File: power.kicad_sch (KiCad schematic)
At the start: 160 parts, among them Q10 SI7613DN-T1-GE3, Q2 BC817-25W, Q3 DZDH0401DW, Q4 DZDH0401DW, Q5 SI7613DN-T1-GE3, Q6 SI7613DN-T1-GE3, Q8 BC817-25W, U1 LT8350RV#PBF, U11 AP22615A_TSOT26, U2 MP2386GG, U3 TPS65983BAZBHR, U9 LM1117MP-3.3_NOPB

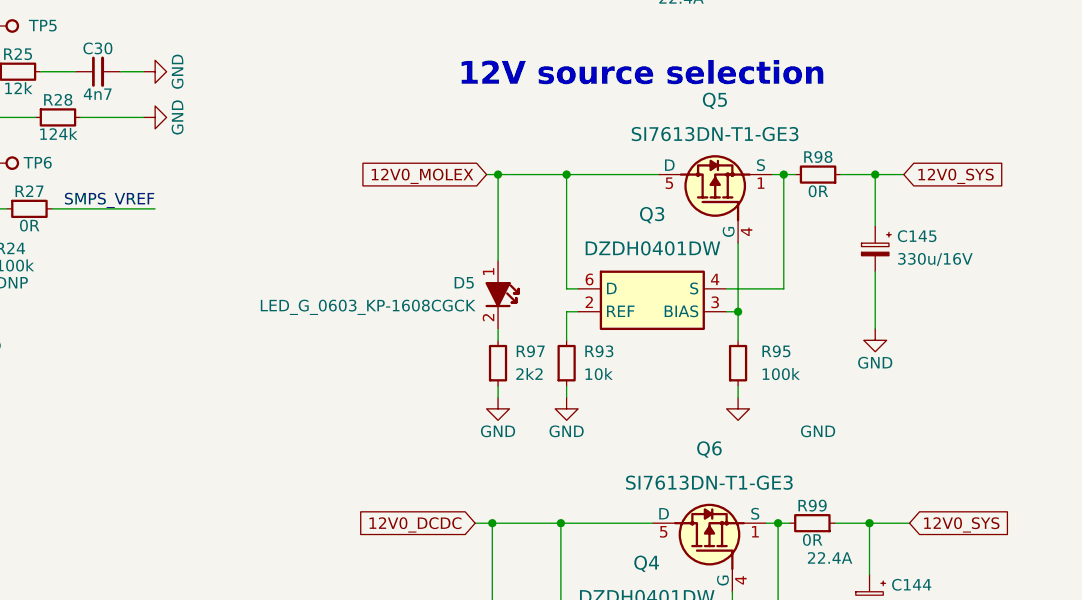
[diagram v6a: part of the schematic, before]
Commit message: Add filtration to 12V0_MOLEX
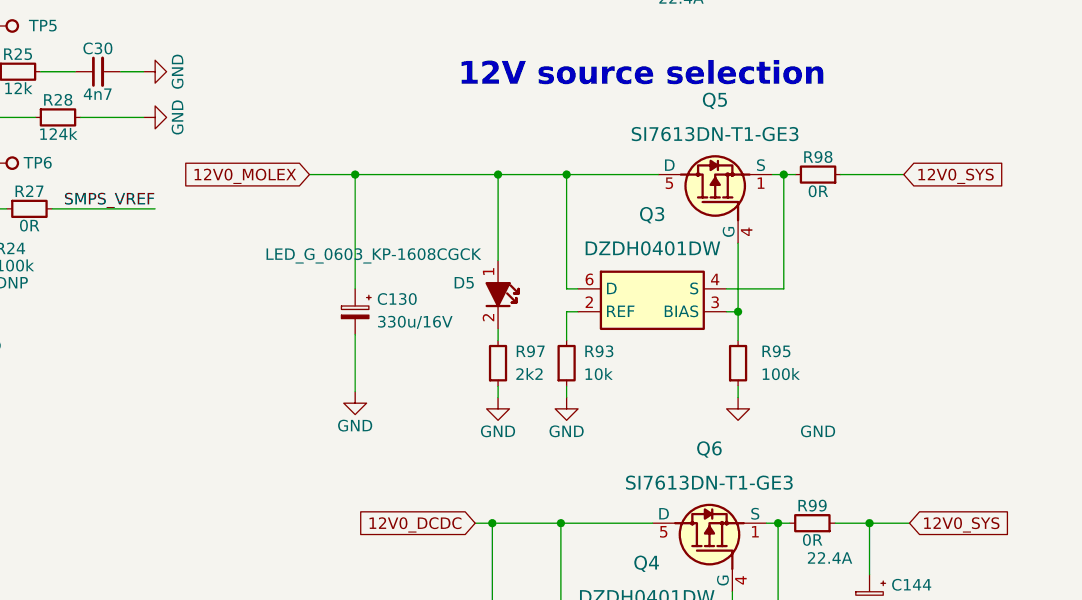
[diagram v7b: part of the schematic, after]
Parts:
- removed C145: C_Pol_330u_16V_KYOCERA-AVX-TCJ-E, antmicro-footprints:C_Pol_EIA-E, symbol antmicroCapacitorspol:C_Pol_330u_16V_KYOCERA-AVX-TCJ-E
- added C130: C_Pol_330u_16V_KYOCERA-AVX-TCJ-E, antmicro-footprints:C_Pol_EIA-E, symbol antmicroCapacitorspol:C_Pol_330u_16V_KYOCERA-AVX-TCJ-E
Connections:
- net 12V0_MOLEX: now also C130.1
- net GND: now also C130.2
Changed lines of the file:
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@@
   (junction (at 118.745 233.045) (diameter 0) (color 0 0 0 0)
   )
+  (junction (at 208.28 262.255) (diameter 0) (color 0 0 0 0)
+  )
   (junction (at 40.005 67.31) (diameter 0) (color 0 0 0 0)
   )
@@
   (junction (at 72.39 46.99) (diameter 0) (color 0 0 0 0)
   )
-  (junction (at 266.065 262.255) (diameter 0) (color 0 0 0 0)
-  )
   (junction (at 85.09 349.25) (diameter 0) (color 0 0 0 0)
   )
@@
   (no_connect (at 73.025 128.27))
   (no_connect (at 107.315 33.02))
+  (wire (pts (xy 208.28 262.255) (xy 224.155 262.255))
+    (stroke (width 0) (type default) (color 0 0 0 0))
+  )
   (wire (pts (xy 259.715 90.805) (xy 259.715 94.615))
     (stroke (width 0) (type default) (color 0 0 0 0))
@@
     (stroke (width 0) (type default) (color 0 0 0 0))
   )
+  (wire (pts (xy 208.28 280.035) (xy 208.28 286.385))
+    (stroke (width 0) (type default) (color 0 0 0 0))
+  )
   (wire (pts (xy 139.7 346.71) (xy 150.495 346.71))
     (stroke (width 0) (type default) (color 0 0 0 0))
@@
     (stroke (width 0) (type default) (color 0 0 0 0))
   )
-  (wire (pts (xy 222.885 262.255) (xy 224.155 262.255))
+  (wire (pts (xy 203.2 262.255) (xy 208.28 262.255))
     (stroke (width 0) (type default) (color 0 0 0 0))
   )
@@
     (stroke (width 0) (type default) (color 0 0 0 0))
   )
-  (wire (pts (xy 266.065 262.255) (xy 269.24 262.255))
-    (stroke (width 0) (type default) (color 0 0 0 0))
-  )
   (wire (pts (xy 220.98 33.02) (xy 232.41 33.02))
     (stroke (width 0) (type default) (color 0 0 0 0))
@@
     (stroke (width 0) (type default) (color 0 0 0 0))
   )
+  (wire (pts (xy 208.28 262.255) (xy 208.28 274.955))
+    (stroke (width 0) (type default) (color 0 0 0 0))
+  )
   (wire (pts (xy 61.595 209.55) (xy 61.595 211.455))
     (stroke (width 0) (type default) (color 0 0 0 0))
@@
     (stroke (width 0) (type default) (color 0 0 0 0))
   )
-  (wire (pts (xy 266.065 273.05) (xy 266.065 279.4))
-    (stroke (width 0) (type default) (color 0 0 0 0))
-  )
   (wire (pts (xy 99.06 253.365) (xy 100.965 253.365))
     (stroke (width 0) (type default) (color 0 0 0 0))
@@
     (stroke (width 0) (type default) (color 0 0 0 0))
   )
-  (wire (pts (xy 262.255 262.255) (xy 266.065 262.255))
+  (wire (pts (xy 262.255 262.255) (xy 269.24 262.255))
     (stroke (width 0) (type default) (color 0 0 0 0))
   )
@@
     (stroke (width 0) (type default) (color 0 0 0 0))
   )
-  (wire (pts (xy 266.065 262.255) (xy 266.065 267.97))
-    (stroke (width 0) (type default) (color 0 0 0 0))
-  )
   (wire (pts (xy 172.72 72.39) (xy 180.34 72.39))
     (stroke (width 0) (type default) (color 0 0 0 0))
@@
     (effects (font (size 1.27 1.27)) (justify left bottom))
   )
-  (global_label "12V0_MOLEX" (shape input) (at 222.885 262.255 180) (fields_autoplaced)
+  (global_label "12V0_MOLEX" (shape input) (at 203.2 262.255 180) (fields_autoplaced)
     (effects (font (size 1.27 1.27)) (justify right))
-    (property "Intersheet References" "${INTERSHEET_REFS}" (id 0) (at 208.6186 262.3344 0)
+    (property "Intersheet References" "${INTERSHEET_REFS}" (id 0) (at 188.9336 262.3344 0)
       (effects (font (size 1.27 1.27)) (justify right) hide)
     )
@@
   )
   (symbol (lib_name "LED_G_0603_KP-1608CGCK_2") (lib_id "thunderbolt-gpu-adapter:LED_G_0603_KP-1608CGCK") (at 224.155 271.78 270) (unit 1)
-    (in_bom yes) (on_board yes) (fields_autoplaced)
+    (in_bom yes) (on_board yes)
     (property "Reference" "D5" (id 0) (at 221.615 274.3199 90)
       (effects (font (size 1.27 1.27) (thickness 0.15)) (justify right))
     )
-    (property "Value" "LED_G_0603_KP-1608CGCK" (id 1) (at 221.615 276.8599 90)
+    (property "Value" "LED_G_0603_KP-1608CGCK" (id 1) (at 222.25 271.145 90)
       (effects (font (size 1.27 1.27) (thickness 0.15)) (justify right))
     )
@@
     (pin "2")
   )
+  (symbol (lib_id "antmicroCapacitorspol:C_Pol_330u_16V_KYOCERA-AVX-TCJ-E") (at 208.28 274.955 270) (unit 1)
+    (in_bom yes) (on_board yes) (fields_autoplaced)
+    (property "Reference" "C130" (id 0) (at 210.693 276.131 90)
+      (effects (font (size 1.27 1.27) (thickness 0.15)) (justify left))
+    )
+    (property "Value" "C_Pol_330u_16V_KYOCERA-AVX-TCJ-E" (id 1) (at 205.74 288.925 0)
+      (effects (font (size 1.27 1.27) (thickness 0.15)) (justify left bottom) hide)
+    )
+    (property "Footprint" "antmicro-footprints:C_Pol_EIA-E" (id 2) (at 200.66 288.925 0)
+      (effects (font (size 1.27 1.27) (thickness 0.15)) (justify left bottom) hide)
+    )
+    (property "Datasheet" "https://datasheets.kyocera-avx.com/TCJ.pdf" (id 3) (at 198.12 288.925 0)
+      (effects (font (size 1.27 1.27) (thickness 0.15)) (justify left bottom) hide)
+    )
+    (property "Val" "330u/16V" (id 4) (at 210.693 278.6547 90)
+      (effects (font (size 1.27 1.27) (thickness 0.15)) (justify left))
+    )
+    (property "MPN" "TCJE337M016R0070E" (id 5) (at 195.58 288.925 0)
+      (effects (font (size 1.27 1.27) (thickness 0.15)) (justify left bottom) hide)
+    )
+    (property "Manufacturer" "KYOCERA AVX" (id 6) (at 193.04 288.925 0)
+      (effects (font (size 1.27 1.27) (thickness 0.15)) (justify left bottom) hide)
+    )
+    (property "License" "Apache-2.0" (id 7) (at 190.5 288.925 0)
+      (effects (font (size 1.27 1.27) (thickness 0.15)) (justify left bottom) hide)
+    )
+    (property "Author" "Antmicro" (id 8) (at 187.96 288.925 0)
+      (effects (font (size 1.27 1.27) (thickness 0.15)) (justify left bottom) hide)
+    )
+    (property "Voltage" "16V" (id 9) (at 185.42 288.925 0)
+      (effects (font (size 1.27 1.27)) (justify left bottom) hide)
+    )
+    (property "Dielectric" "template_dielectric" (id 10) (at 182.88 288.925 0)
+      (effects (font (size 1.27 1.27)) (justify left bottom) hide)
+    )
+    (pin "1")
+    (pin "2")
+  )
   (symbol (lib_name "TP_1mm_SMD_6") (lib_id "thunderbolt-gpu-adapter:TP_1mm_SMD") (at 74.295 328.93 90) (unit 1)
     (in_bom yes) (on_board yes)
@@
     (pin "1")
   )
+  (symbol (lib_id "thunderbolt-gpu-adapter:GND") (at 208.28 286.385 0) (unit 1)
+    (in_bom yes) (on_board yes)
+    (property "Reference" "#PWR0197" (id 0) (at 208.28 292.735 0)
+      (effects (font (size 1.27 1.27)) hide)
+    )
+    (property "Value" "GND" (id 1) (at 208.28 290.195 0))
+    (property "Footprint" "" (id 2) (at 208.28 286.385 0)
+      (effects (font (size 1.27 1.27)) hide)
+    )
+    (property "Datasheet" "" (id 3) (at 208.28 286.385 0)
+      (effects (font (size 1.27 1.27)) hide)
+    )
+    (property "Author" "Antmicro" (id 4) (at 217.17 294.005 0)
+      (effects (font (size 1.27 1.27) (thickness 0.15)) (justify left bottom) hide)
+    )
+    (property "License" "Apache-2.0" (id 5) (at 217.17 296.545 0)
+      (effects (font (size 1.27 1.27) (thickness 0.15)) (justify left bottom) hide)
+    )
+    (pin "1")
+  )
   (symbol (lib_id "thunderbolt-gpu-adapter:BLM21SN300SZ1D") (at 193.675 41.91 0) (mirror x) (unit 1)
     (in_bom yes) (on_board yes)
@@
     (pin "1")
   )
-  (symbol (lib_id "antmicroCapacitorspol:C_Pol_330u_16V_KYOCERA-AVX-TCJ-E") (at 266.065 267.97 270) (unit 1)
-    (in_bom yes) (on_board yes) (fields_autoplaced)
-    (property "Reference" "C145" (id 0) (at 268.478 269.146 90)
-      (effects (font (size 1.27 1.27) (thickness 0.15)) (justify left))
-    )
-    (property "Value" "C_Pol_330u_16V_KYOCERA-AVX-TCJ-E" (id 1) (at 263.525 281.94 0)
-      (effects (font (size 1.27 1.27) (thickness 0.15)) (justify left bottom) hide)
-    )
-    (property "Footprint" "antmicro-footprints:C_Pol_EIA-E" (id 2) (at 258.445 281.94 0)
-      (effects (font (size 1.27 1.27) (thickness 0.15)) (justify left bottom) hide)
-    )
-    (property "Datasheet" "https://datasheets.kyocera-avx.com/TCJ.pdf" (id 3) (at 255.905 281.94 0)
-      (effects (font (size 1.27 1.27) (thickness 0.15)) (justify left bottom) hide)
-    )
-    (property "Val" "330u/16V" (id 4) (at 268.478 271.6697 90)
-      (effects (font (size 1.27 1.27) (thickness 0.15)) (justify left))
-    )
-    (property "MPN" "TCJE337M016R0070E" (id 5) (at 253.365 281.94 0)
-      (effects (font (size 1.27 1.27) (thickness 0.15)) (justify left bottom) hide)
-    )
-    (property "Manufacturer" "KYOCERA AVX" (id 6) (at 250.825 281.94 0)
-      (effects (font (size 1.27 1.27) (thickness 0.15)) (justify left bottom) hide)
-    )
-    (property "License" "Apache-2.0" (id 7) (at 248.285 281.94 0)
-      (effects (font (size 1.27 1.27) (thickness 0.15)) (justify left bottom) hide)
-    )
-    (property "Author" "Antmicro" (id 8) (at 245.745 281.94 0)
-      (effects (font (size 1.27 1.27) (thickness 0.15)) (justify left bottom) hide)
-    )
-    (property "Voltage" "16V" (id 9) (at 243.205 281.94 0)
-      (effects (font (size 1.27 1.27)) (justify left bottom) hide)
-    )
-    (property "Dielectric" "template_dielectric" (id 10) (at 240.665 281.94 0)
-      (effects (font (size 1.27 1.27)) (justify left bottom) hide)
-    )
-    (pin "1")
-    (pin "2")
-  )
   (symbol (lib_name "C_100n_0402_4") (lib_id "thunderbolt-gpu-adapter:C_100n_0402") (at 93.345 337.82 90) (unit 1)
     (in_bom yes) (on_board yes)
@@
     )
     (pin "1")
-  )
-  (symbol (lib_id "thunderbolt-gpu-adapter:GND") (at 266.065 279.4 0) (unit 1)
-    (in_bom yes) (on_board yes)
-    (property "Reference" "#PWR0224" (id 0) (at 266.065 285.75 0)
-      (effects (font (size 1.27 1.27)) hide)
-    )
-    (property "Value" "GND" (id 1) (at 266.065 283.21 0))
-    (property "Footprint" "" (id 2) (at 266.065 279.4 0)
-      (effects (font (size 1.27 1.27)) hide)
-    )
-    (property "Datasheet" "" (id 3) (at 266.065 279.4 0)
-      (effects (font (size 1.27 1.27)) hide)
-    )
-    (property "Author" "Antmicro" (id 4) (at 274.955 287.02 0)
-      (effects (font (size 1.27 1.27) (thickness 0.15)) (justify left bottom) hide)
-    )
-    (property "License" "Apache-2.0" (id 5) (at 274.955 289.56 0)
-      (effects (font (size 1.27 1.27) (thickness 0.15)) (justify left bottom) hide)
-    )
-    (pin "1")
